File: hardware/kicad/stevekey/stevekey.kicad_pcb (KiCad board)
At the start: 2 copper layers, 21 parts, among them J1 ATMEL-ICE-10, J2 Conn_01x04, J3 Conn_01x02, J4 Conn_01x02, J5 Conn_01x02, SW1 SW_SL, SW2 SW_CAPS, SW3 SW_4080, U1 CD4066BE, U2 ATtiny214-SS

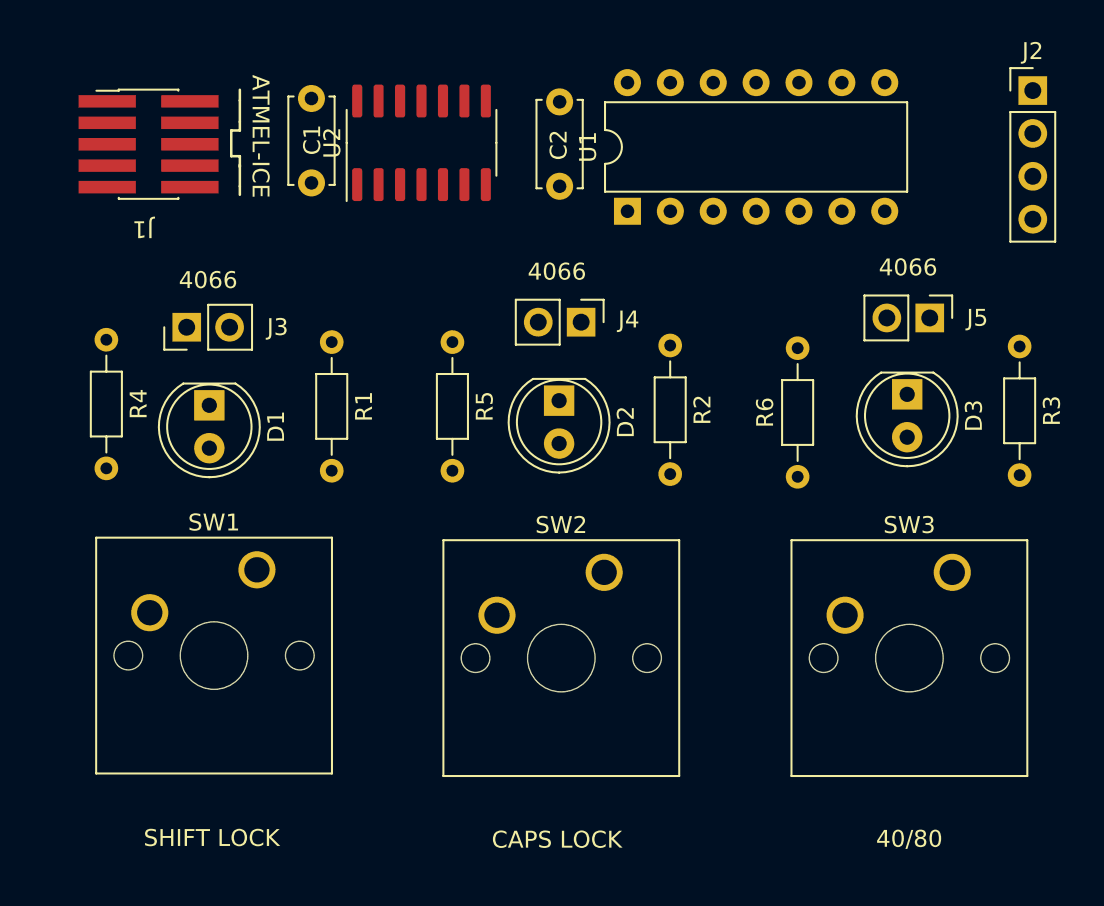
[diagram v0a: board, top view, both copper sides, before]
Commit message: Initial routing is complete
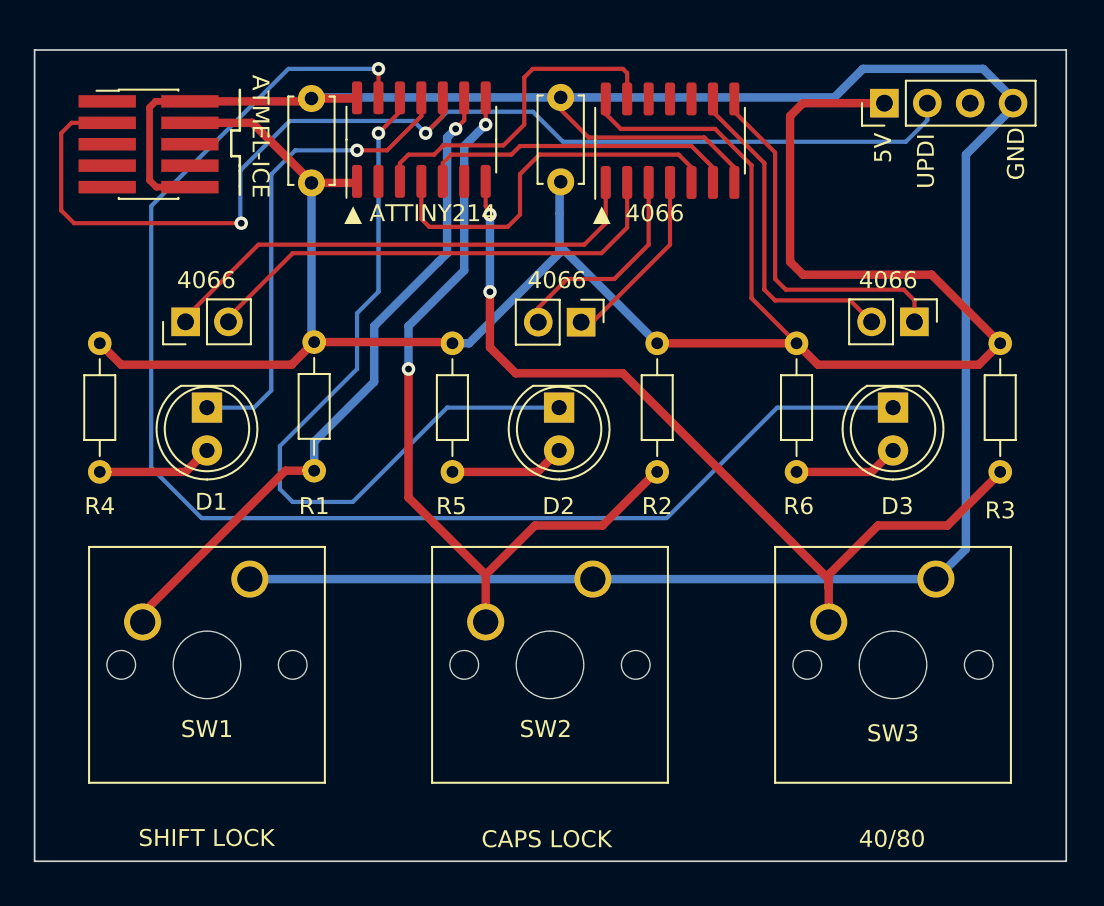
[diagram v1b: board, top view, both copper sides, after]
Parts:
- U1: value CD4066BE -> CD4066BM; footprint Package_DIP:DIP-14_W7.62mm -> Package_SO:SO-14_3.9x8.65mm_P1.27mm
- moved J2 8.82 mm to (158.2, 74.7), turned to 90 degrees
- moved R6 7.91 mm to (153.0, 88.9), turned to -90 degrees
- moved U1 4.88 mm to (145.5, 76.9)
- moved R3 1.17 mm to (165.1, 88.9)
- moved D3 1.15 mm to (158.8, 92.7)
- moved SW3 1.05 mm to (161.3, 102.9)
- moved R1 1.04 mm to (124.5, 88.8)
- moved J5 0.93 mm to (160.0, 87.6)
- moved R2 0.78 mm to (144.8, 88.9)
- moved SW2 0.78 mm to (141.0, 102.9)
- moved SW1 0.69 mm to (120.7, 102.9)
- moved R4 0.44 mm to (111.8, 88.9)
- moved D2 0.41 mm to (139.0, 92.7)
- moved J3 0.33 mm to (116.8, 87.6)
- moved C2 0.27 mm to (139.1, 79.3)
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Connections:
- J2 pad 1: unconnected-(J2-Pin_1-Pad1) -> VCC
- J2 pad 2: unconnected-(J2-Pin_2-Pad2) -> UPDI
- J2 pad 4: unconnected-(J2-Pin_4-Pad4) -> GND
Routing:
- net GND: track 0.00 -> 147.8 mm
- net VCC: track 0.00 -> 136.3 mm
- net /N4080LED: track 0.00 -> 81.9 mm, vias 0 -> 1
- net UPDI: track 0.00 -> 69.5 mm, vias 0 -> 2
- net N4080KEY: track 0.00 -> 52.2 mm, vias 0 -> 2
- net NCAPSKEY: track 0.00 -> 47.8 mm, vias 0 -> 2
- net /NCAPSLED: track 0.00 -> 45.3 mm, vias 0 -> 1
- net NSLKEY: track 0.00 -> 39.9 mm, vias 0 -> 1
- net Net-(J3-Pin_1): track 0.00 -> 29.9 mm
- net Net-(J3-Pin_2): track 0.00 -> 28.8 mm
- net /NSLLED: track 0.00 -> 28.4 mm, vias 0 -> 1
- net CAPSOUT: track 0.00 -> 22.8 mm
- net Net-(J5-Pin_1): track 0.00 -> 21.7 mm
- net SLOUT: track 0.00 -> 20.1 mm
- net Net-(J5-Pin_2): track 0.00 -> 19.7 mm
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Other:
- board outline added: 61.1 x 48.1 mm
- board text added: "5V"
- board text added: "GND"
- board text added: "UPDI"
- board text added: "▲ 4066"
- board text added: "▲ ATTINY214"

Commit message: Add transistor to pull /RES down
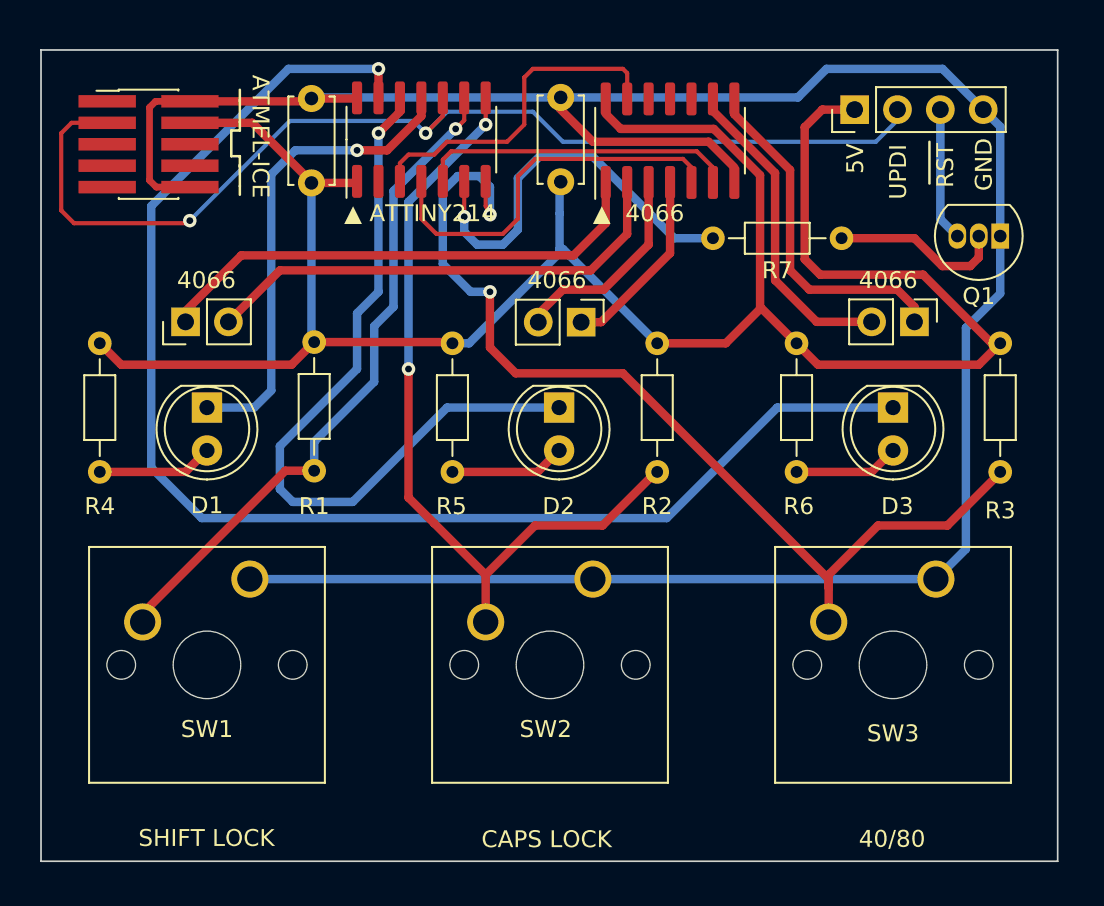
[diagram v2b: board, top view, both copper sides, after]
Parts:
- added Q1: 2N3904, Package_TO_SOT_THT:TO-92_Inline, F.Cu at (165.1, 82.5)
- added R7: 1K, Resistor_THT:R_Axial_DIN0204_L3.6mm_D1.6mm_P7.62mm_Horizontal, F.Cu at (148.1, 82.7)
- moved J2 1.81 mm to (156.5, 75.1)
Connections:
- J2 pad 3: unconnected-(J2-Pin_3-Pad3) -> Net-(J2-Pin_3)
- U2 pad 6: unconnected-(U2-PB3-Pad6) -> CBMRESETOUT
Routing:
- net CBMRESETOUT: track 0.00 -> 24.2 mm, vias 0 -> 1
- net Net-(Q1-B): track 0.00 -> 10.3 mm
- net N4080KEY: track 52.2 -> 60.5 mm
- net Net-(J2-Pin_3): track 0.00 -> 7.91 mm
- net VCC: track 136.3 -> 131.0 mm
- net UPDI: track 69.5 -> 65.4 mm
- net GND: track 147.8 -> 145.4 mm
- net Net-(J5-Pin_1): track 21.7 -> 20.7 mm
- net Net-(J5-Pin_2): track 19.7 -> 19.0 mm
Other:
- board size 61.1 x 48.1 mm -> 60.2 x 48.1 mm
- board text added: "RST"

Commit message: Bring the extra 4066 pins out to the header
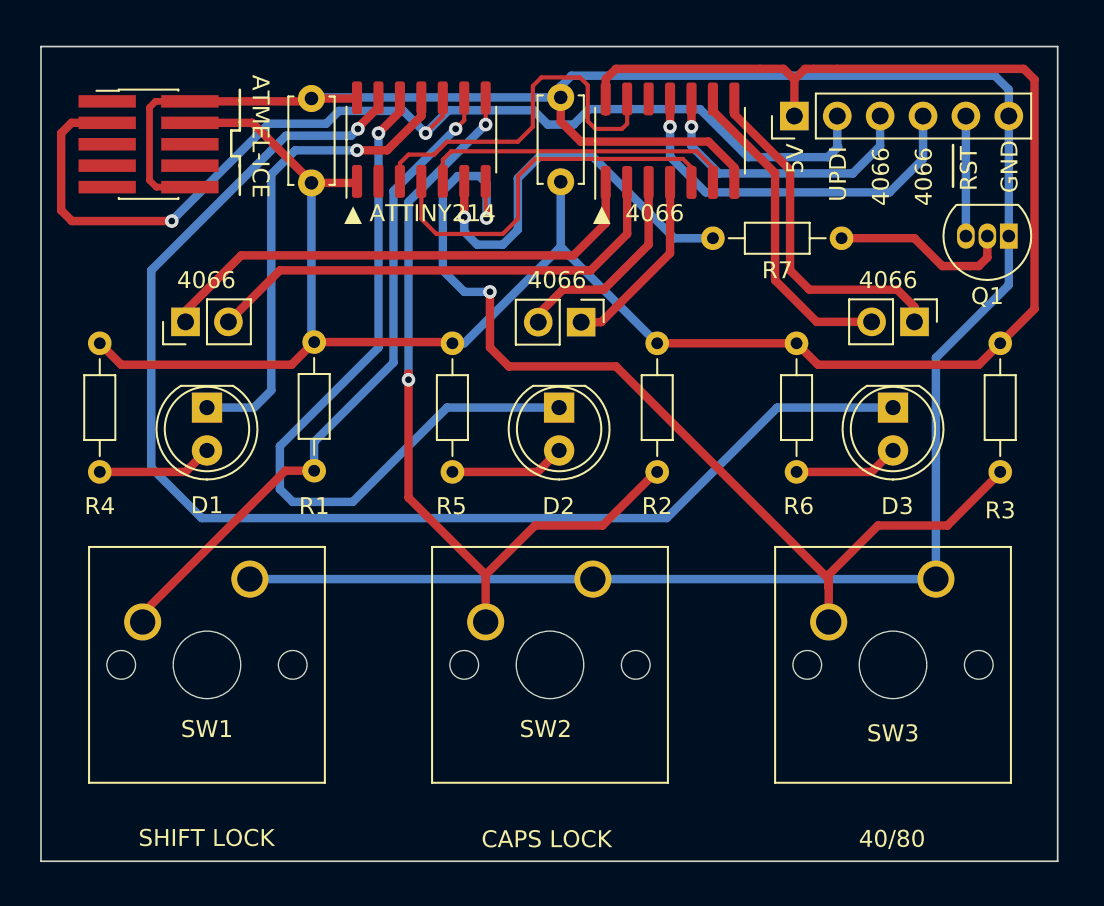
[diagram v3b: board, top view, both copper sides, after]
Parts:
- J2: footprint Connector_PinHeader_2.54mm:PinHeader_1x04_P2.54mm_Vertical -> Connector_PinHeader_2.54mm:PinHeader_1x06_P2.54mm_Vertical
- moved J2 3.59 mm to (152.9, 75.4)
- moved Q1 0.51 mm to (165.6, 82.5)
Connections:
- J2 pad 3: Net-(J2-Pin_3) -> EXTRA1
- J2 pad 4: GND -> EXTRA0
- Q1 pad 3: Net-(J2-Pin_3) -> Net-(J2-Pin_5)
- U1 pad 10: unconnected-(U1-Pad10) -> EXTRA1
- U1 pad 11: unconnected-(U1-Pad11) -> EXTRA0
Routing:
- net EXTRA0: track 0.00 -> 22.6 mm, vias 0 -> 1
- net EXTRA1: track 0.00 -> 17.1 mm, vias 0 -> 1
- net Net-(J2-Pin_3): track 7.91 -> 0.00 mm
- net Net-(J2-Pin_5): track 0.00 -> 7.11 mm
- net /N4080LED: track 81.9 -> 77.8 mm
- net GND: track 145.4 -> 148.5 mm
- net SLOUT: track 20.1 -> 22.2 mm
- net VCC: track 131.0 -> 132.0 mm
- net UPDI: track 65.4 -> 64.4 mm
- net N4080KEY: track 60.5 -> 61.3 mm
- net Net-(Q1-B): track 10.3 -> 10.8 mm
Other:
- board size 60.2 x 48.1 mm -> 60.2 x 48.3 mm
- board text added: "STEVEKEY MCU DEV BOARD REV. 1 © 2023 MIKE NABEREZNY"

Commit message: Add capacitor on input power
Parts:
- added C3: 10uF, Capacitor_THT:CP_Radial_D6.3mm_P2.50mm, F.Cu at (165.8, 83.2)
- C1, C2: value C_Small -> 0.1uF
- moved Q1 6.07 mm to (159.5, 82.5)
- moved R7 1.57 mm to (146.9, 83.8)
- moved J3 0.87 mm to (116.8, 88.5)
- moved J5 0.87 mm to (160.0, 88.5)
- moved J4 0.85 mm to (140.3, 88.5)
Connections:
- U1 pad 12: unconnected-(U1-Pad12) -> EXOUT
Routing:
- net EXOUT: track 0.00 -> 37.2 mm, vias 0 -> 2
- net VCC: track 132.0 -> 138.5 mm
- net Net-(Q1-B): track 10.8 -> 5.78 mm
- net GND: track 148.5 -> 152.6 mm
- net Net-(J2-Pin_5): track 7.11 -> 9.74 mm
- net EXTRA0: track 22.6 -> 21.2 mm
- net Net-(J4-Pin_1): track 11.1 -> 12.2 mm
- net Net-(J4-Pin_2): track 12.4 -> 13.1 mm
- net N4080KEY: track 61.3 -> 60.7 mm
- net EXTRA1: track 17.1 -> 16.5 mm
- net Net-(J5-Pin_1): track 20.7 -> 21.2 mm
- net Net-(J5-Pin_2): track 19.0 -> 18.5 mm
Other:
- board size 60.2 x 48.3 mm -> 60.4 x 49.1 mm
